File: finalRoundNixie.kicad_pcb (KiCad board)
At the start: 2 copper layers, 37 x 56.3 mm, 64 parts, among them J1 Conn_01x06_Male, J2 HV_IN, J3 Conn_01x06_Female, J4 HV_OUT, Q1 MMBTA42LT1, Q10 MMBTA42LT1, Q11 AO3400, Q12 AO3400, Q13 AO3400, Q14 MMBTA42LT1, Q15 MMBTA42LT1, Q2 MMBTA42LT1, Q3 MMBTA42LT1, Q4 MMBTA42LT1, Q5 MMBTA42LT1, Q6 MMBTA42LT1, Q7 MMBTA42LT1, Q8 MMBTA42LT1, Q9 MMBTA42LT1, U1 74HC595D, U2 nixie-tube, U3 74HC595D, U4 ams1117-5.0

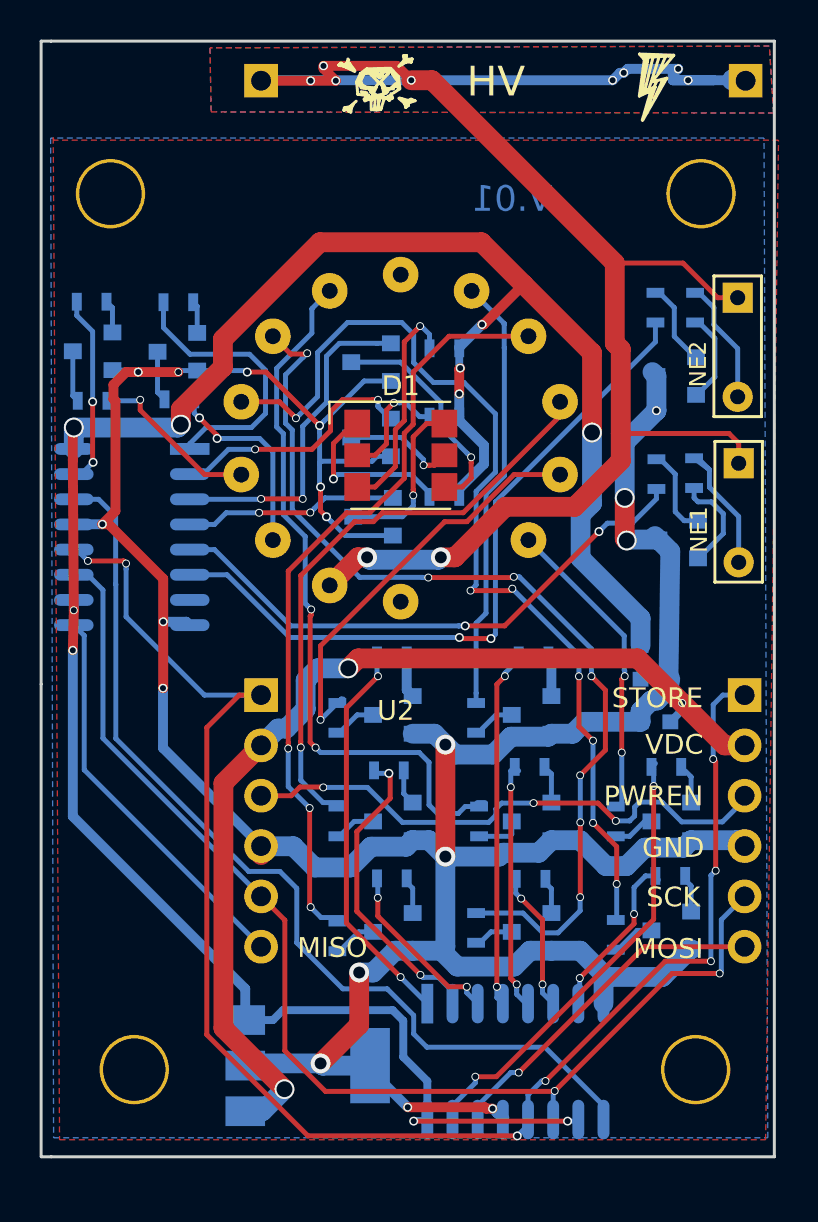
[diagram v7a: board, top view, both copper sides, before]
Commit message: added few things
lightning symbol on neon and around nixie tube
via stiching
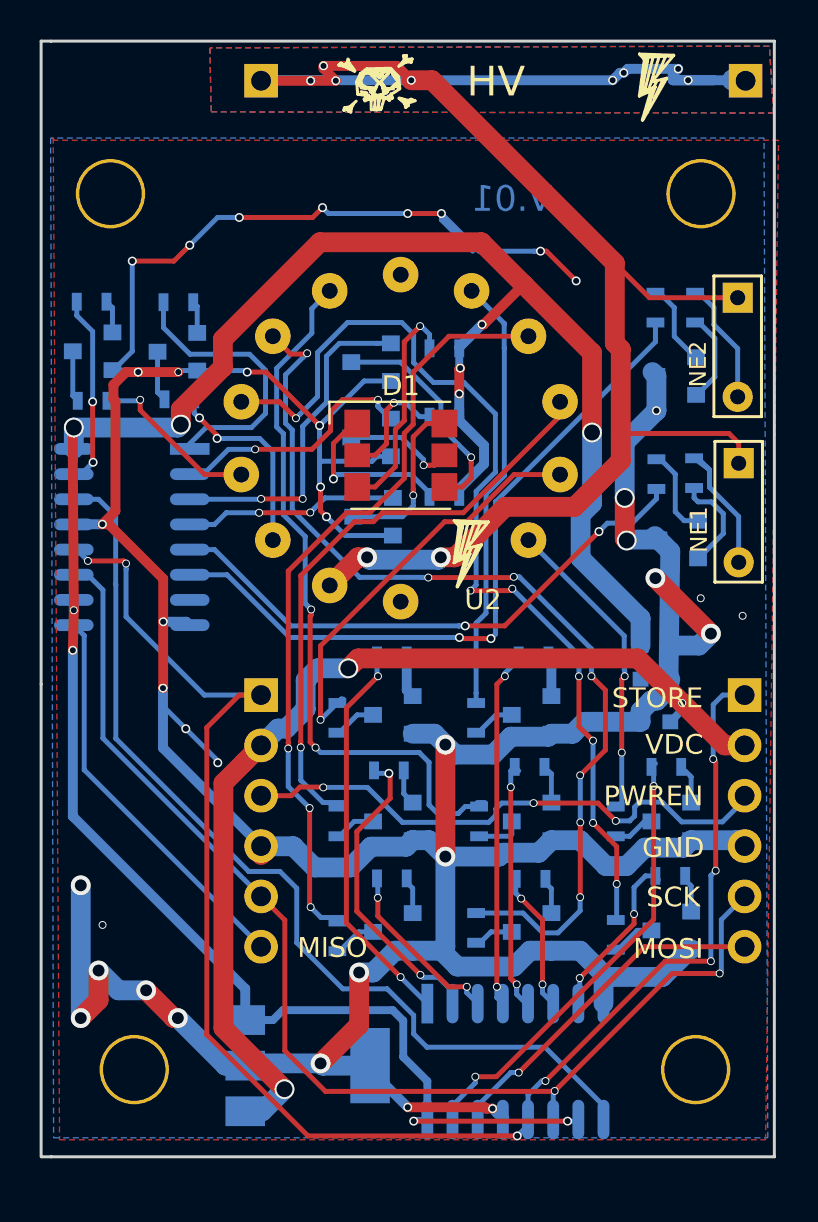
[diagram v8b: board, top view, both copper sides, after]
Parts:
- added Z?: lightning, nixie-tube-fp:lightning, B.Cu at (186.6, 64.1)
- added Z?: lightning, nixie-tube-fp:lightning, F.Cu at (173.1, 66.0)
- added Z?: lightning, nixie-tube-fp:lightning, B.Cu at (186.5, 55.7)
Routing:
- net GND: track 175.3 -> 238.9 mm, vias 18 -> 35
- net (no net): vias 0 -> 3
